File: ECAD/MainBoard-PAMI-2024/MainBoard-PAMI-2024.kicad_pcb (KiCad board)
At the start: 2 copper layers, 79.5 x 96 mm, 37 parts, among them J1 Selecteur-Robot, J10 Serial, J2 USB_B, J3 Tirette, J4 Servo, J5 Sensor_Right, J6 Sensor_Left, J7 LeftMotor, J8 RightMotor, J9 color_team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

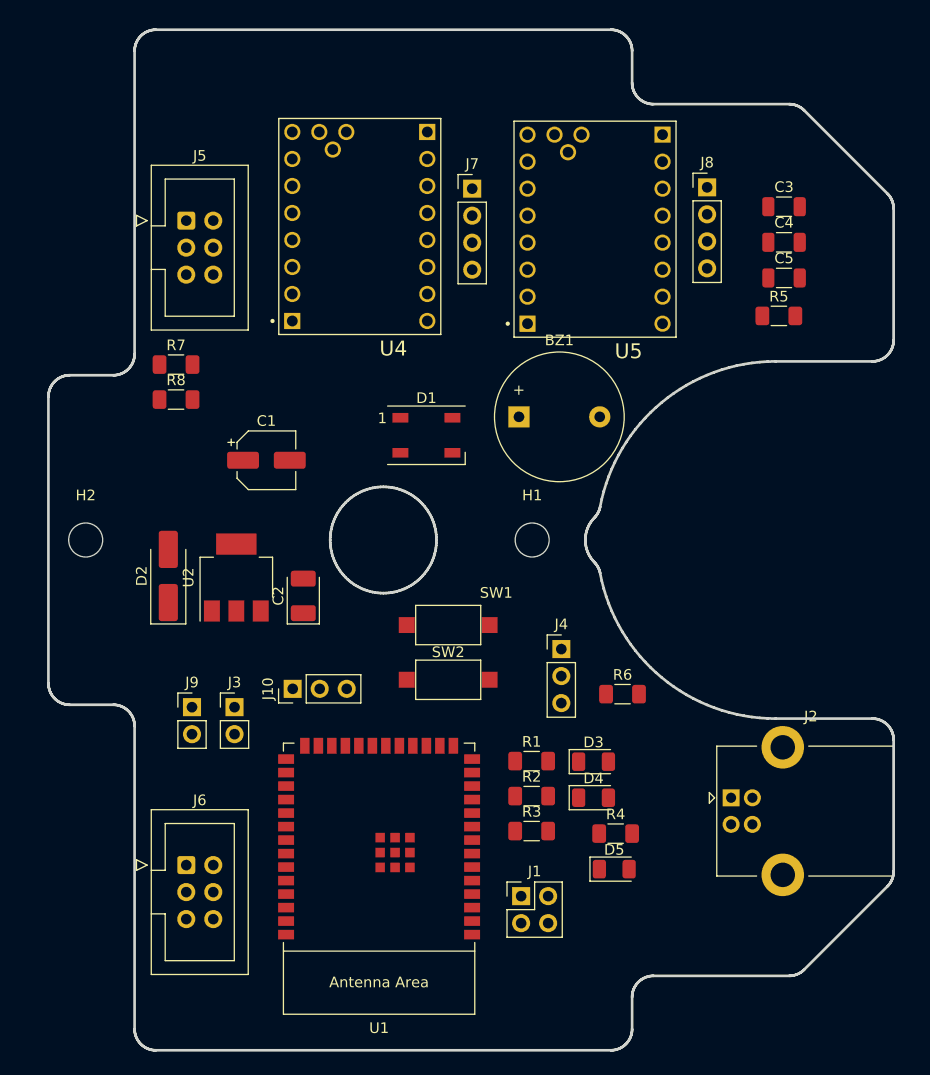
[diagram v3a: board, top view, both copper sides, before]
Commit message: New version
- Wire pins
- Add PCB way
- Change Cutout
- Update 3D
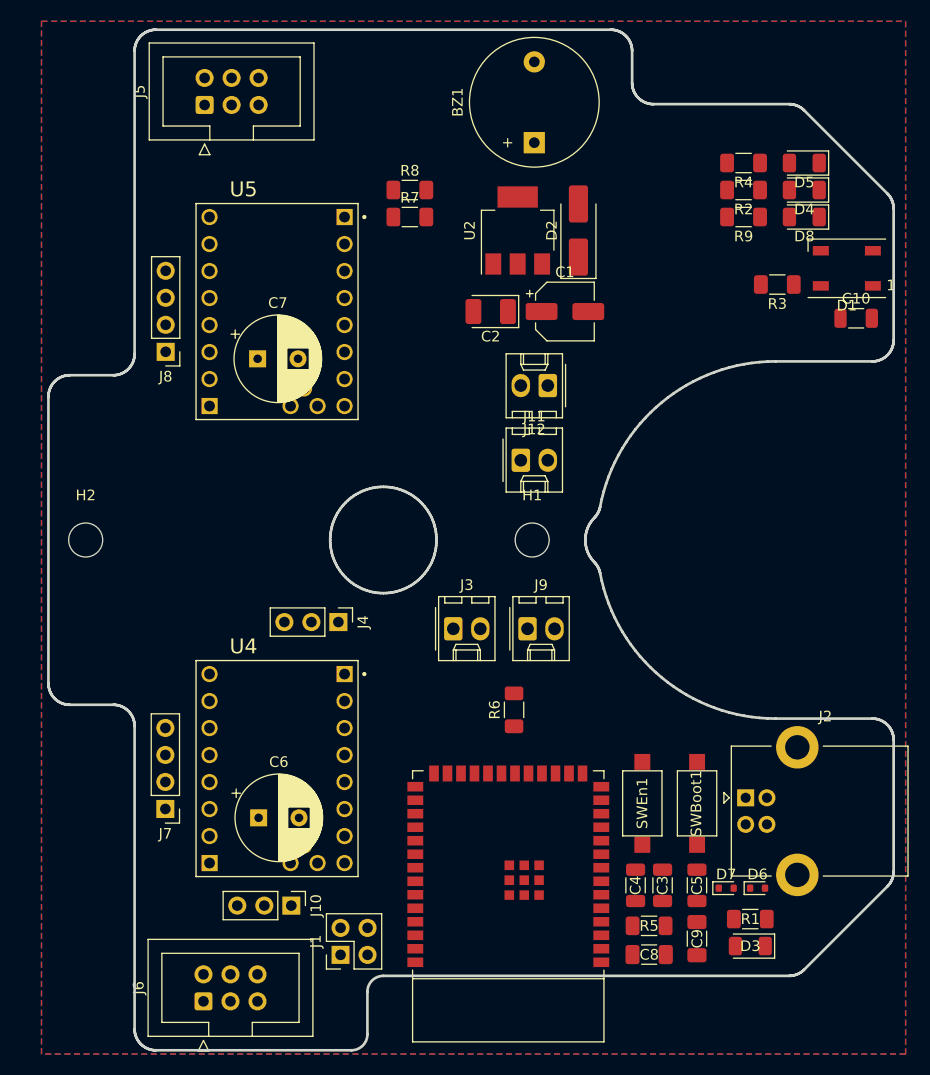
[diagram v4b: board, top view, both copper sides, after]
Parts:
- removed SW1: SW_EN, Button_Switch_SMD:SW_SPST_CK_RS282G05A3
- removed SW2: SW_Boot, Button_Switch_SMD:SW_SPST_CK_RS282G05A3
- added C10: 0.1uF, Capacitor_SMD:C_1206_3216Metric, F.Cu at (170.0, 80.6)
- added C6: 100uF, Capacitor_THT:CP_Radial_D8.0mm_P3.80mm, F.Cu at (113.8, 127.6)
- added C7: 100uF, Capacitor_THT:CP_Radial_D8.0mm_P3.80mm, F.Cu at (113.7, 84.5)
- added C8: 0.1uF, Capacitor_SMD:C_1206_3216Metric_Pad1.33x1.80mm_HandSolder, F.Cu at (150.5, 140.5)
- added C9: 10uF, Capacitor_SMD:C_1206_3216Metric_Pad1.33x1.80mm_HandSolder, F.Cu at (155.0, 139.0)
- added D6: D_TVS_Bidirectional_Generic, Diode_SMD:D_SOD-523, F.Cu at (160.7, 134.2)
- added D7: D_TVS_Bidirectional_Generic, Diode_SMD:D_SOD-523, F.Cu at (157.8, 134.2)
- added D8: Red, LED_SMD:LED_1206_3216Metric, F.Cu at (165.1, 71.1)
- added J11: Con_Batt, Connector_Molex:Molex_KK-254_AE-6410-02A_1x02_P2.54mm_Vertical, F.Cu at (138.4, 94.0)
- added J12: BAU, Connector_Molex:Molex_KK-254_AE-6410-02A_1x02_P2.54mm_Vertical, F.Cu at (141.0, 87.0)
- added R9: 1K, Resistor_SMD:R_1206_3216Metric_Pad1.30x1.75mm_HandSolder, F.Cu at (159.4, 71.1)
- added SWBoot1: SW_Boot, Button_Switch_SMD:SW_SPST_CK_RS282G05A3, F.Cu at (155.0, 126.3)
- added SWEn1: SW_EN, Button_Switch_SMD:SW_SPST_CK_RS282G05A3, F.Cu at (149.9, 126.3)
- J3, J9: footprint Connector_PinHeader_2.54mm:PinHeader_1x02_P2.54mm_Vertical -> Connector_Molex:Molex_KK-254_AE-6410-02A_1x02_P2.54mm_Vertical
- moved D5 68.8 mm to (165.1, 66.0), turned to 180 degrees
- moved J7 65.1 mm to (105.0, 126.8), turned to 180 degrees
- moved C3 64.8 mm to (151.8, 134.0), turned to -90 degrees
- moved R4 64.2 mm to (159.4, 66.0), turned to 180 degrees
- moved C4 62.1 mm to (149.2, 134.0), turned to -90 degrees
- moved D4 60.5 mm to (165.1, 68.6), turned to 180 degrees
- moved R2 60.4 mm to (159.4, 68.6), turned to 180 degrees
- moved R5 58.7 mm to (150.5, 137.8), turned to 180 degrees
- moved C5 57.7 mm to (155.0, 134.0), turned to -90 degrees
- moved R3 56.4 mm to (162.6, 77.5), turned to 180 degrees
- moved J8 53.2 mm to (105.0, 83.8), turned to 180 degrees
- moved U4 51.6 mm to (115.5, 123.0), turned to 0 degrees
- moved D2 50.4 mm to (143.8, 72.4)
- moved D1 42.6 mm to (169.1, 75.9), turned to 180 degrees
- moved U2 42.0 mm to (138.1, 72.4)
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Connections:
- U1 pad 10: unconnected-(U1-GPIO17/U1TXD/ADC2_CH6-Pad10) -> DAC1
- U1 pad 11: unconnected-(U1-GPIO18/U1RXD/ADC2_CH7/CLK_OUT3-Pad11) -> DAC2
- U1 pad 12: unconnected-(U1-GPIO8/TOUCH8/ADC1_CH7/SUBSPICS1-Pad12) -> SDA
- U1 pad 15: unconnected-(U1-GPIO3/TOUCH3/ADC1_CH2-Pad15) -> XSHUT_RIGHT
- U1 pad 17: unconnected-(U1-GPIO9/TOUCH9/ADC1_CH8/FSPIHD/SUBSPIHD-Pad17) -> SCL
- U1 pad 18: unconnected-(U1-GPIO10/TOUCH10/ADC1_CH9/FSPICS0/FSPIIO4/SUBSPICS0-Pad18) -> RightDir
- U1 pad 19: unconnected-(U1-GPIO11/TOUCH11/ADC2_CH0/FSPID/FSPIIO5/SUBSPID-Pad19) -> RightStep
- U1 pad 20: unconnected-(U1-GPIO12/TOUCH12/ADC2_CH1/FSPICLK/FSPIIO6/SUBSPICLK-Pad20) -> Servo
- U1 pad 21: unconnected-(U1-GPIO13/TOUCH13/ADC2_CH2/FSPIQ/FSPIIO7/SUBSPIQ-Pad21) -> LeftDir
- U1 pad 22: unconnected-(U1-GPIO14/TOUCH14/ADC2_CH3/FSPIWP/FSPIDQS/SUBSPIWP-Pad22) -> LeftStep
- U1 pad 23: unconnected-(U1-GPIO21-Pad23) -> LeftMS2
- U1 pad 24: unconnected-(U1-GPIO47/SPICLK_P/SUBSPICLK_P_DIFF-Pad24) -> LeftMS1
- U1 pad 25: unconnected-(U1-GPIO48/SPICLK_N/SUBSPICLK_N_DIFF-Pad25) -> EnDriver
- U1 pad 31: unconnected-(U1-GPIO38/FSPIWP/SUBSPIWP-Pad31) -> XSHUT_LEFT
- U1 pad 38: SCL -> BotNum01
- U1 pad 39: SDA -> BotNum02
- U1 pad 5: unconnected-(U1-GPIO5/TOUCH5/ADC1_CH4-Pad5) -> LED_Status
- U1 pad 6: unconnected-(U1-GPIO6/TOUCH6/ADC1_CH5-Pad6) -> Color_Team
- U1 pad 7: unconnected-(U1-GPIO7/TOUCH7/ADC1_CH6-Pad7) -> Tirette
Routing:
- added copper zone on B.Cu, net GND
- added copper zone on F.Cu, net GND
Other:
- outline, holes or cut-outs redrawn
